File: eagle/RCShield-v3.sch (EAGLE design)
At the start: 53 parts, among them J1/J2 JOYSTICKPTH, P1/P3 POT, P2/P4 POT, Q1 MMBT3906, U1 TOUSCRUINO_SHIELD, U2 FT232RL-BASICSSOP, U4 XBEE, X1 USB

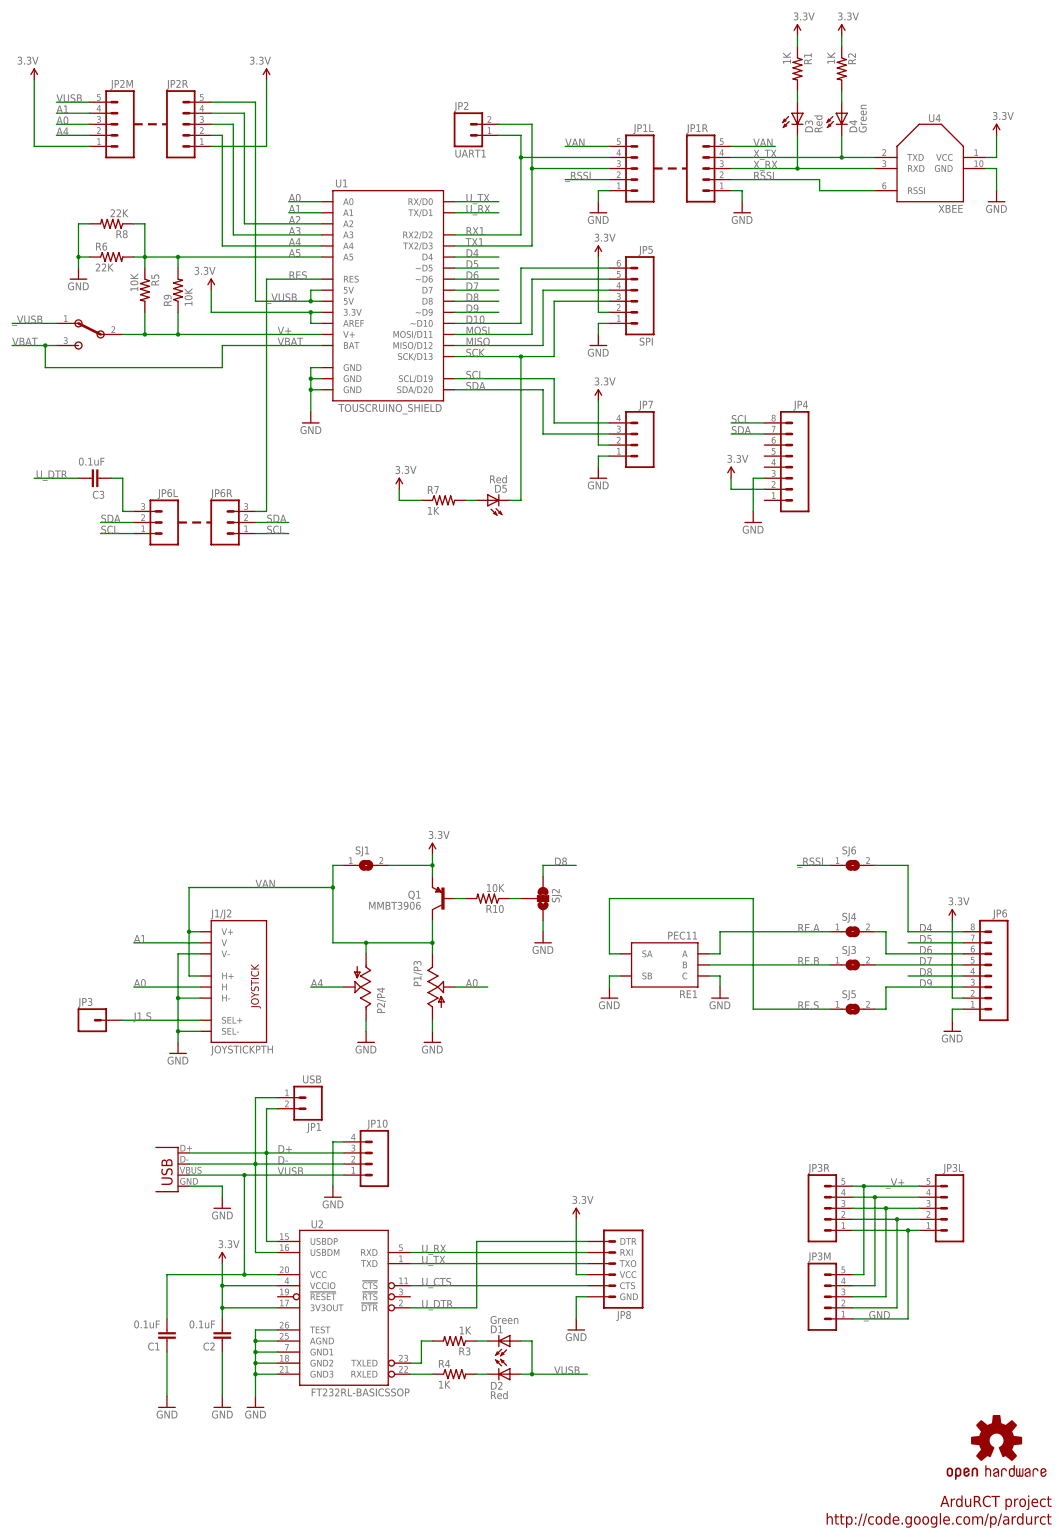
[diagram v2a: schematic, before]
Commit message: 
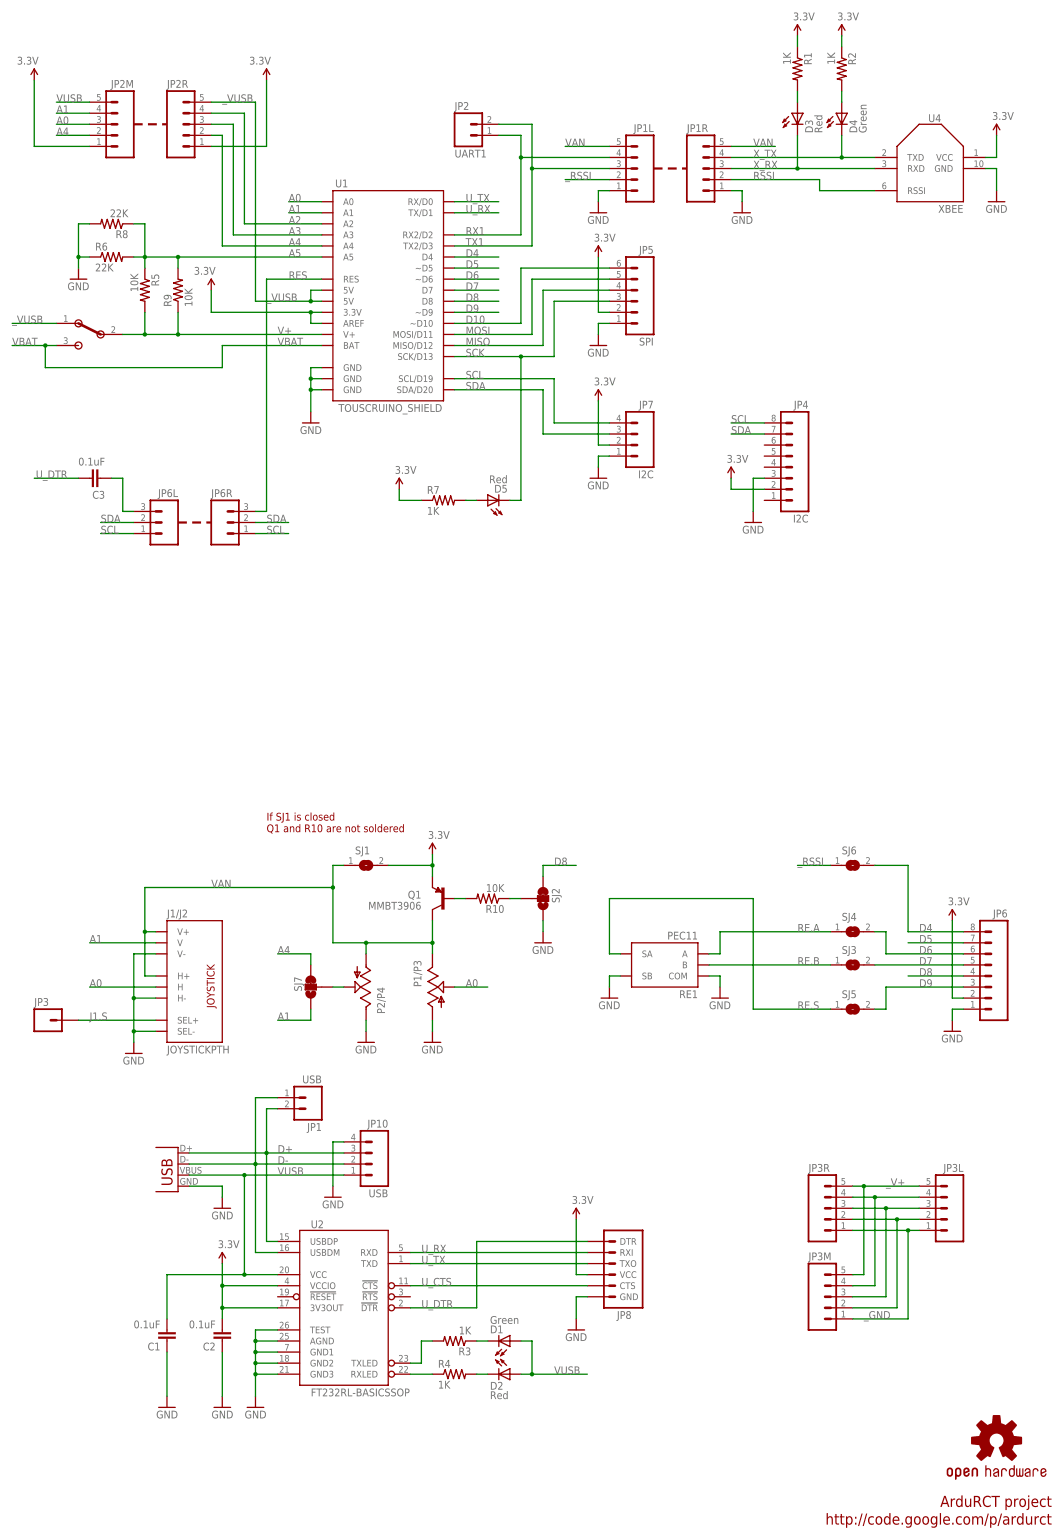
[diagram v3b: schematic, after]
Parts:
- added SJ7: SJ_2WAYS_1-2W, wibauxl:SJ_2WAYS_1-2W
- JP10: value M04 -> USB
- JP4: value M08 -> I2C
- JP7: value M04 -> I2C
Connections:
- new net N$7: P2/P4.S, SJ7.2
- net A1: now also SJ7.3
- net A4: now also SJ7.1; no longer P2/P4.S
- net GND: now also RE1.COM; no longer RE1.C
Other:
- note added: "If SJ1 is closed Q1 and R10 are not soldered"
- moved on the sheet: J1/J2, JP3
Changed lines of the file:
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@@
 <part name="R10" library="SparkFun" deviceset="RESISTOR" device="0805-RES" value="10K"/>
 <part name="P+17" library="SparkFun" deviceset="3.3V" device=""/>
-<part name="JP7" library="wibauxl" deviceset="M04" device="" value=""/>
-<part name="JP4" library="wibauxl" deviceset="M08" device="" value=""/>
+<part name="JP7" library="wibauxl" deviceset="M04" device="" value="I2C"/>
+<part name="JP4" library="wibauxl" deviceset="M08" device="" value="I2C"/>
 <part name="GND12" library="SparkFun" deviceset="GND" device=""/>
 <part name="P+4" library="SparkFun" deviceset="3.3V" device=""/>
-<part name="JP10" library="wibauxl" deviceset="M04" device="" value=""/>
+<part name="JP10" library="wibauxl" deviceset="M04" device="" value="USB"/>
 <part name="GND13" library="SparkFun" deviceset="GND" device=""/>
 <part name="GND16" library="SparkFun" deviceset="GND" device=""/>
 <part name="JP1" library="wibauxl" deviceset="M02" device="" value="USB"/>
 <part name="SJ1" library="wibauxl" deviceset="SJ" device=""/>
+<part name="SJ7" library="wibauxl" deviceset="SJ_2WAYS_1-2" device="W" value=""/>
 </parts>
 <sheets>
@@
 <text x="243.84" y="21.336" size="2.54" layer="94" ratio="12" rot="R180">http://code.google.com/p/ardurct</text>
 <wire x1="43.18" y1="248.92" x2="50.8" y2="248.92" width="0.508" layer="94" style="shortdash"/>
+<text x="63.5" y="177.8" size="1.778" layer="94">If SJ1 is closed
+Q1 and R10 are not soldered</text>
 </plain>
 <instances>
@@
 <instance part="U2" gate="G$1" x="81.28" y="68.58"/>
 <instance part="U4" gate="G$1" x="215.9" y="330.2" rot="MR0"/>
-<instance part="J1/J2" gate="G$1" x="58.42" y="144.78"/>
+<instance part="J1/J2" gate="G$1" x="48.26" y="144.78"/>
 <instance part="X1" gate="G$1" x="43.18" y="96.52" rot="MR0"/>
 <instance part="GND3" gate="1" x="53.34" y="91.44" rot="MR0"/>
@@
 <instance part="D3" gate="G$1" x="185.42" y="342.9"/>
 <instance part="R1" gate="G$1" x="185.42" y="353.06" rot="R270"/>
-<instance part="GND24" gate="1" x="43.18" y="127"/>
+<instance part="GND24" gate="1" x="33.02" y="127"/>
 <instance part="GND4" gate="1" x="134.62" y="63.5"/>
 <instance part="P+1" gate="G$1" x="134.62" y="88.9"/>
@@
 <instance part="GND11" gate="1" x="167.64" y="139.7"/>
 <instance part="JP2" gate="G$1" x="111.76" y="337.82"/>
-<instance part="JP3" gate="G$1" x="22.86" y="134.62"/>
+<instance part="JP3" gate="G$1" x="12.7" y="134.62"/>
 <instance part="SJ2" gate="G$1" x="127" y="162.56" rot="MR0"/>
 <instance part="Q1" gate="G$1" x="104.14" y="162.56" rot="MR0"/>
@@
 <instance part="JP1" gate="G$1" x="71.12" y="116.84" rot="R180"/>
 <instance part="SJ1" gate="1" x="86.36" y="170.18"/>
+<instance part="SJ7" gate="G$1" x="73.66" y="142.24"/>
 </instances>
 <busses>
@@
 </segment>
 <segment>
-<wire x1="48.26" y1="149.86" x2="43.18" y2="149.86" width="0.1524" layer="91"/>
-<wire x1="43.18" y1="149.86" x2="43.18" y2="139.7" width="0.1524" layer="91"/>
-<wire x1="43.18" y1="139.7" x2="43.18" y2="132.08" width="0.1524" layer="91"/>
-<wire x1="48.26" y1="132.08" x2="43.18" y2="132.08" width="0.1524" layer="91"/>
-<wire x1="48.26" y1="139.7" x2="43.18" y2="139.7" width="0.1524" layer="91"/>
-<wire x1="43.18" y1="132.08" x2="43.18" y2="129.54" width="0.1524" layer="91"/>
-<junction x="43.18" y="139.7"/>
-<junction x="43.18" y="132.08"/>
+<wire x1="38.1" y1="149.86" x2="33.02" y2="149.86" width="0.1524" layer="91"/>
+<wire x1="33.02" y1="149.86" x2="33.02" y2="139.7" width="0.1524" layer="91"/>
+<wire x1="33.02" y1="139.7" x2="33.02" y2="132.08" width="0.1524" layer="91"/>
+<wire x1="38.1" y1="132.08" x2="33.02" y2="132.08" width="0.1524" layer="91"/>
+<wire x1="38.1" y1="139.7" x2="33.02" y2="139.7" width="0.1524" layer="91"/>
+<wire x1="33.02" y1="132.08" x2="33.02" y2="129.54" width="0.1524" layer="91"/>
+<junction x="33.02" y="139.7"/>
+<junction x="33.02" y="132.08"/>
 <pinref part="J1/J2" gate="G$1" pin="V-"/>
 <pinref part="J1/J2" gate="G$1" pin="SEL-"/>
@@
 </segment>
 <segment>
-<pinref part="RE1" gate="G$1" pin="C"/>
+<pinref part="RE1" gate="G$1" pin="COM"/>
 <wire x1="165.1" y1="144.78" x2="167.64" y2="144.78" width="0.1524" layer="91"/>
 <wire x1="167.64" y1="144.78" x2="167.64" y2="142.24" width="0.1524" layer="91"/>
@@
 </segment>
 <segment>
-<wire x1="48.26" y1="142.24" x2="33.02" y2="142.24" width="0.1524" layer="91"/>
-<label x="33.02" y="142.24" size="1.778" layer="95"/>
+<wire x1="38.1" y1="142.24" x2="22.86" y2="142.24" width="0.1524" layer="91"/>
+<label x="22.86" y="142.24" size="1.778" layer="95"/>
 <pinref part="J1/J2" gate="G$1" pin="H"/>
 </segment>
@@
 </segment>
 <segment>
-<wire x1="48.26" y1="152.4" x2="33.02" y2="152.4" width="0.1524" layer="91"/>
-<label x="33.02" y="152.4" size="1.778" layer="95"/>
+<wire x1="38.1" y1="152.4" x2="22.86" y2="152.4" width="0.1524" layer="91"/>
+<label x="22.86" y="152.4" size="1.778" layer="95"/>
 <pinref part="J1/J2" gate="G$1" pin="V"/>
+</segment>
+<segment>
+<pinref part="SJ7" gate="G$1" pin="3"/>
+<wire x1="73.66" y1="137.16" x2="73.66" y2="134.62" width="0.1524" layer="91"/>
+<wire x1="73.66" y1="134.62" x2="66.04" y2="134.62" width="0.1524" layer="91"/>
+<label x="66.04" y="134.62" size="1.778" layer="95"/>
 </segment>
 </net>
@@
 <net name="A4" class="0">
 <segment>
-<wire x1="81.28" y1="142.24" x2="73.66" y2="142.24" width="0.1524" layer="91"/>
-<label x="73.66" y="142.24" size="1.778" layer="95"/>
-<pinref part="P2/P4" gate="G$1" pin="S"/>
+<wire x1="73.66" y1="149.86" x2="66.04" y2="149.86" width="0.1524" layer="91"/>
+<label x="66.04" y="149.86" size="1.778" layer="95"/>
+<pinref part="SJ7" gate="G$1" pin="1"/>
+<wire x1="73.66" y1="149.86" x2="73.66" y2="147.32" width="0.1524" layer="91"/>
 </segment>
 <segment>
@@
 <net name="J1.S" class="0">
 <segment>
-<wire x1="48.26" y1="134.62" x2="30.48" y2="134.62" width="0.1524" layer="91"/>
-<label x="33.02" y="134.62" size="1.778" layer="95"/>
+<wire x1="38.1" y1="134.62" x2="20.32" y2="134.62" width="0.1524" layer="91"/>
+<label x="22.86" y="134.62" size="1.778" layer="95"/>
 <pinref part="J1/J2" gate="G$1" pin="SEL+"/>
 <pinref part="JP3" gate="G$1" pin="1"/>
@@
 <wire x1="73.66" y1="302.26" x2="73.66" y2="299.72" width="0.1524" layer="91"/>
 <junction x="73.66" y="299.72"/>
+<label x="53.34" y="345.44" size="1.778" layer="95"/>
 </segment>
 <segment>
@@
 <net name="VAN" class="0">
 <segment>
-<wire x1="45.72" y1="154.94" x2="48.26" y2="154.94" width="0.1524" layer="91"/>
-<wire x1="45.72" y1="154.94" x2="45.72" y2="144.78" width="0.1524" layer="91"/>
-<wire x1="45.72" y1="144.78" x2="48.26" y2="144.78" width="0.1524" layer="91"/>
-<junction x="45.72" y="154.94"/>
+<wire x1="35.56" y1="154.94" x2="38.1" y2="154.94" width="0.1524" layer="91"/>
+<wire x1="35.56" y1="154.94" x2="35.56" y2="144.78" width="0.1524" layer="91"/>
+<wire x1="35.56" y1="144.78" x2="38.1" y2="144.78" width="0.1524" layer="91"/>
+<junction x="35.56" y="154.94"/>
 <pinref part="J1/J2" gate="G$1" pin="H+"/>
 <pinref part="J1/J2" gate="G$1" pin="V+"/>
-<wire x1="45.72" y1="154.94" x2="45.72" y2="165.1" width="0.1524" layer="91"/>
+<wire x1="35.56" y1="154.94" x2="35.56" y2="165.1" width="0.1524" layer="91"/>
 <wire x1="86.36" y1="149.86" x2="86.36" y2="152.4" width="0.1524" layer="91"/>
 <pinref part="P2/P4" gate="G$1" pin="A"/>
@@
 <pinref part="Q1" gate="G$1" pin="C"/>
 <wire x1="101.6" y1="157.48" x2="101.6" y2="152.4" width="0.1524" layer="91"/>
-<wire x1="45.72" y1="165.1" x2="78.74" y2="165.1" width="0.1524" layer="91"/>
+<wire x1="35.56" y1="165.1" x2="78.74" y2="165.1" width="0.1524" layer="91"/>
 <wire x1="78.74" y1="165.1" x2="78.74" y2="152.4" width="0.1524" layer="91"/>
 <wire x1="78.74" y1="152.4" x2="86.36" y2="152.4" width="0.1524" layer="91"/>
 <junction x="86.36" y="152.4"/>
-<label x="60.96" y="165.1" size="1.778" layer="95"/>
+<label x="50.8" y="165.1" size="1.778" layer="95"/>
 <wire x1="78.74" y1="165.1" x2="78.74" y2="170.18" width="0.1524" layer="91"/>
 <pinref part="SJ1" gate="1" pin="1"/>
@@
 <pinref part="SJ2" gate="G$1" pin="2"/>
 <wire x1="119.38" y1="162.56" x2="121.92" y2="162.56" width="0.1524" layer="91"/>
+</segment>
+</net>
+<net name="N$7" class="0">
+<segment>
+<pinref part="SJ7" gate="G$1" pin="2"/>
+<wire x1="78.74" y1="142.24" x2="81.28" y2="142.24" width="0.1524" layer="91"/>
+<pinref part="P2/P4" gate="G$1" pin="S"/>
 </segment>
 </net>
@@
 </schematic>
 </drawing>
+<compatibility>
+<note version="6.3" minversion="6.2.2" severity="warning">
+Since Version 6.2.2 text objects can contain more than one line,
+which will not be processed correctly with this version.
+</note>
+</compatibility>
 </eagle>
